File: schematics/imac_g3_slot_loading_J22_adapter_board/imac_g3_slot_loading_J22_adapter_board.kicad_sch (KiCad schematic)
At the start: 8 parts

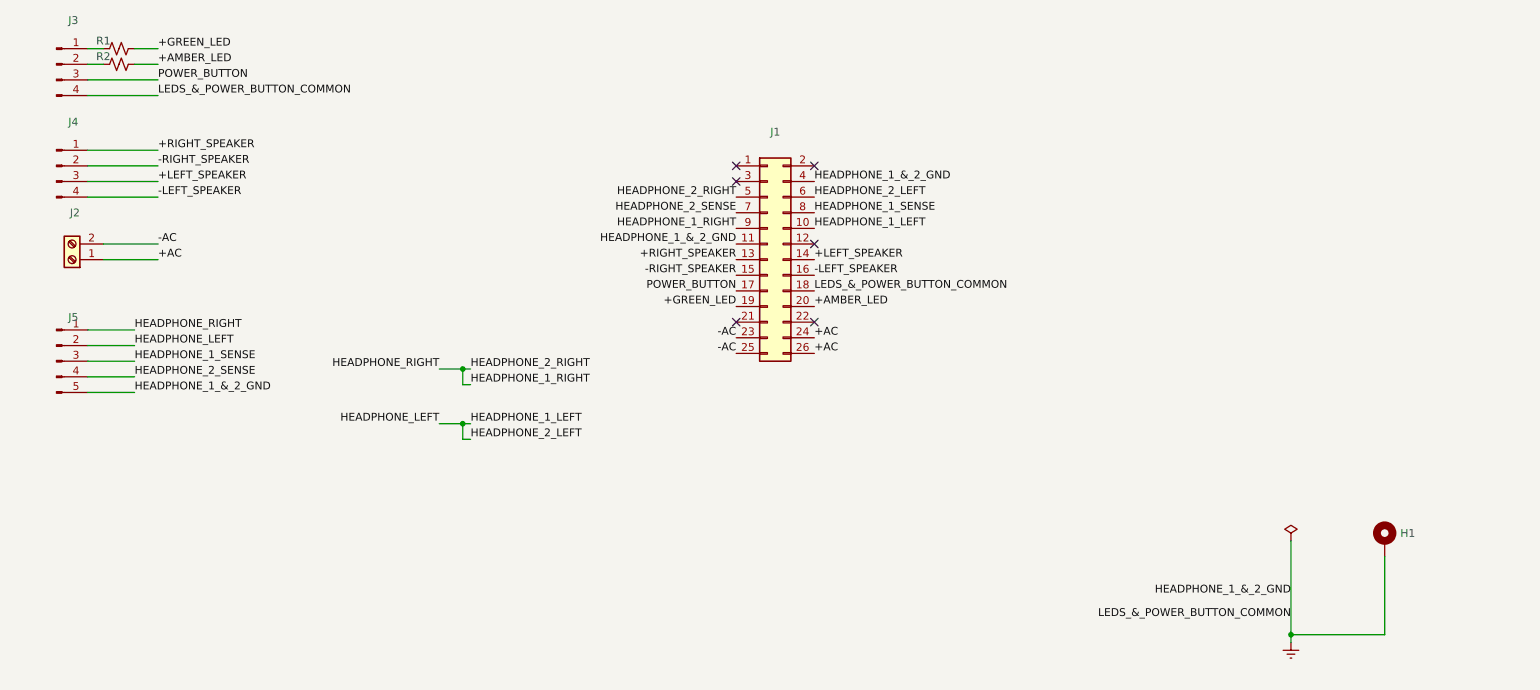
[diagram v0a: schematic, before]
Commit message: Update part numbers
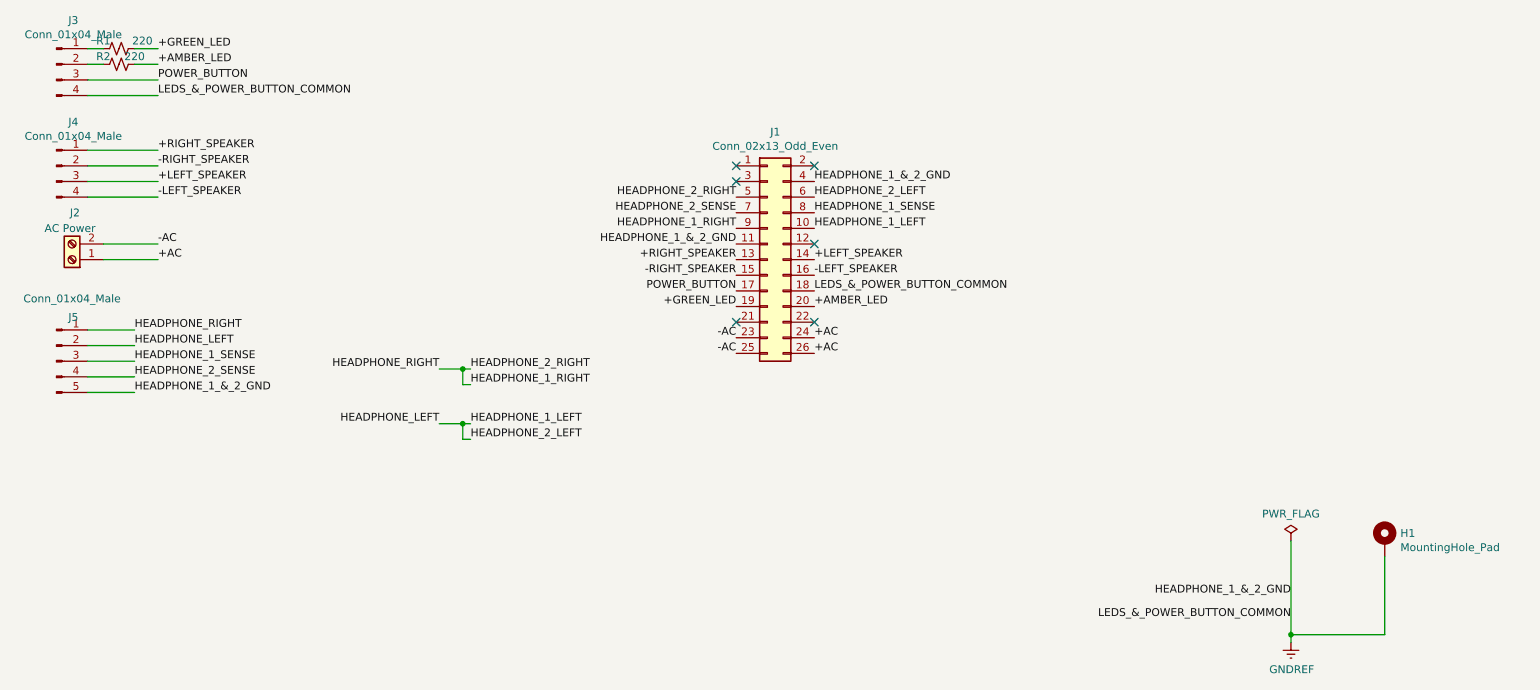
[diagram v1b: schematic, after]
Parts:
- H1: value (none) -> MountingHole_Pad; footprint (none) -> MountingHole:MountingHole_3.5mm_Pad_Via
- J1: value (none) -> Conn_02x13_Odd_Even; footprint (none) -> Connector_PinHeader_2.54mm:PinHeader_2x13_P2.54mm_Vertical
- J2: value (none) -> AC Power; footprint (none) -> TerminalBlock_Phoenix:TerminalBlock_Phoenix_PT-1,5-2-5.0-H_1x02_P5.00mm_Horizontal
- J3, J4: value (none) -> Conn_01x04_Male; footprint (none) -> Connector_JST:JST_XH_B4B-XH-A_1x04_P2.50mm_Vertical
- J5: value (none) -> Conn_01x04_Male; footprint (none) -> Connector_JST:JST_XH_B5B-XH-A_1x05_P2.50mm_Vertical
- R1, R2: value (none) -> 220; footprint (none) -> Resistor_THT:R_Axial_DIN0207_L6.3mm_D2.5mm_P7.62mm_Horizontal
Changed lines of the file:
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@@
     (in_bom yes) (on_board yes)
     (property "Reference" "J1" (id 0) (at 139.7 35.1282 0))
-    (property "Value" "" (id 1) (at 139.7 37.4396 0))
-    (property "Footprint" "" (id 2) (at 138.43 55.88 0)
+    (property "Value" "Conn_02x13_Odd_Even" (id 1) (at 139.7 37.4396 0))
+    (property "Footprint" "Connector_PinHeader_2.54mm:PinHeader_2x13_P2.54mm_Vertical" (id 2) (at 138.43 55.88 0)
       (effects (font (size 1.27 1.27)) hide)
     )
@@
       (effects (font (size 1.27 1.27)) (justify left))
     )
-    (property "Value" "" (id 1) (at 241.3 102.6668 0)
+    (property "Value" "MountingHole_Pad" (id 1) (at 241.3 102.6668 0)
       (effects (font (size 1.27 1.27)) (justify left))
     )
-    (property "Footprint" "" (id 2) (at 238.76 101.6 0)
+    (property "Footprint" "MountingHole:MountingHole_3.5mm_Pad_Via" (id 2) (at 238.76 101.6 0)
       (effects (font (size 1.27 1.27)) hide)
     )
@@
       (effects (font (size 1.27 1.27)) hide)
     )
-    (property "Value" "" (id 1) (at 223.647 122.5042 0))
+    (property "Value" "GNDREF" (id 1) (at 223.647 122.5042 0))
     (property "Footprint" "" (id 2) (at 223.52 118.11 0)
       (effects (font (size 1.27 1.27)) hide)
@@
     (in_bom yes) (on_board yes)
     (property "Reference" "R2" (id 0) (at 30.48 22.86 90))
-    (property "Value" "" (id 1) (at 35.56 22.86 90))
-    (property "Footprint" "" (id 2) (at 33.02 24.13 0)
+    (property "Value" "220" (id 1) (at 35.56 22.86 90))
+    (property "Footprint" "Resistor_THT:R_Axial_DIN0207_L6.3mm_D2.5mm_P7.62mm_Horizontal" (id 2) (at 33.02 24.13 0)
       (effects (font (size 1.27 1.27)) hide)
     )
@@
     (in_bom yes) (on_board yes)
     (property "Reference" "R1" (id 0) (at 30.48 20.32 90))
-    (property "Value" "" (id 1) (at 36.83 20.32 90))
-    (property "Footprint" "" (id 2) (at 33.02 21.59 0)
+    (property "Value" "220" (id 1) (at 36.83 20.32 90))
+    (property "Footprint" "Resistor_THT:R_Axial_DIN0207_L6.3mm_D2.5mm_P7.62mm_Horizontal" (id 2) (at 33.02 21.59 0)
       (effects (font (size 1.27 1.27)) hide)
     )
@@
       (effects (font (size 1.27 1.27)) hide)
     )
-    (property "Value" "" (id 1) (at 223.52 97.2058 0))
+    (property "Value" "PWR_FLAG" (id 1) (at 223.52 97.2058 0))
     (property "Footprint" "" (id 2) (at 223.52 101.6 0)
       (effects (font (size 1.27 1.27)) hide)
@@
       (effects (font (size 1.27 1.27)) (justify left))
     )
-    (property "Value" "" (id 1) (at 29.21 50.8 0)
+    (property "Value" "AC Power" (id 1) (at 29.21 50.8 0)
       (effects (font (size 1.27 1.27)) (justify left))
     )
-    (property "Footprint" "" (id 2) (at 25.4 55.88 0)
+    (property "Footprint" "TerminalBlock_Phoenix:TerminalBlock_Phoenix_PT-1,5-2-5.0-H_1x02_P5.00mm_Horizontal" (id 2) (at 25.4 55.88 0)
       (effects (font (size 1.27 1.27)) hide)
     )
@@
     (in_bom yes) (on_board yes)
     (property "Reference" "J3" (id 0) (at 25.6032 16.9926 0))
-    (property "Value" "" (id 1) (at 25.6032 19.304 0))
-    (property "Footprint" "" (id 2) (at 22.86 24.13 0)
+    (property "Value" "Conn_01x04_Male" (id 1) (at 25.6032 19.304 0))
+    (property "Footprint" "Connector_JST:JST_XH_B4B-XH-A_1x04_P2.50mm_Vertical" (id 2) (at 22.86 24.13 0)
       (effects (font (size 1.27 1.27)) hide)
     )
@@
     (in_bom yes) (on_board yes)
     (property "Reference" "J4" (id 0) (at 25.6032 33.5026 0))
-    (property "Value" "" (id 1) (at 25.6032 35.814 0))
-    (property "Footprint" "" (id 2) (at 22.86 40.64 0)
+    (property "Value" "Conn_01x04_Male" (id 1) (at 25.6032 35.814 0))
+    (property "Footprint" "Connector_JST:JST_XH_B4B-XH-A_1x04_P2.50mm_Vertical" (id 2) (at 22.86 40.64 0)
       (effects (font (size 1.27 1.27)) hide)
     )
@@
     (in_bom yes) (on_board yes)
     (property "Reference" "J5" (id 0) (at 25.6032 65.2526 0))
-    (property "Value" "" (id 1) (at 25.4 62.23 0))
-    (property "Footprint" "" (id 2) (at 22.86 72.39 0)
+    (property "Value" "Conn_01x04_Male" (id 1) (at 25.4 62.23 0))
+    (property "Footprint" "Connector_JST:JST_XH_B5B-XH-A_1x05_P2.50mm_Vertical" (id 2) (at 22.86 72.39 0)
       (effects (font (size 1.27 1.27)) hide)
     )
